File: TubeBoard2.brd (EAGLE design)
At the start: 155 x 114 mm, 2 parts

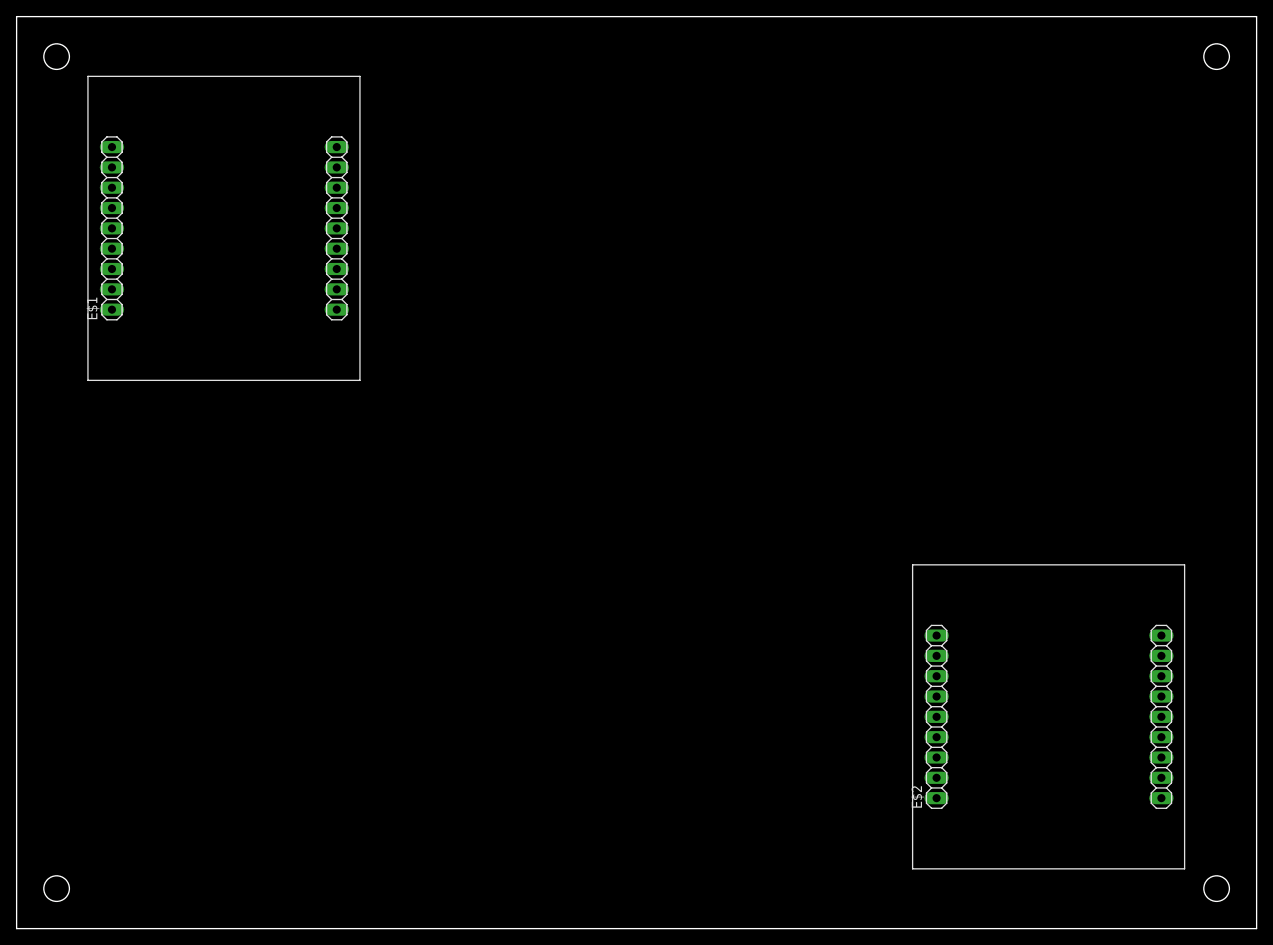
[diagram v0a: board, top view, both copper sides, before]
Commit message: [fix]真空管の場所を少し変更
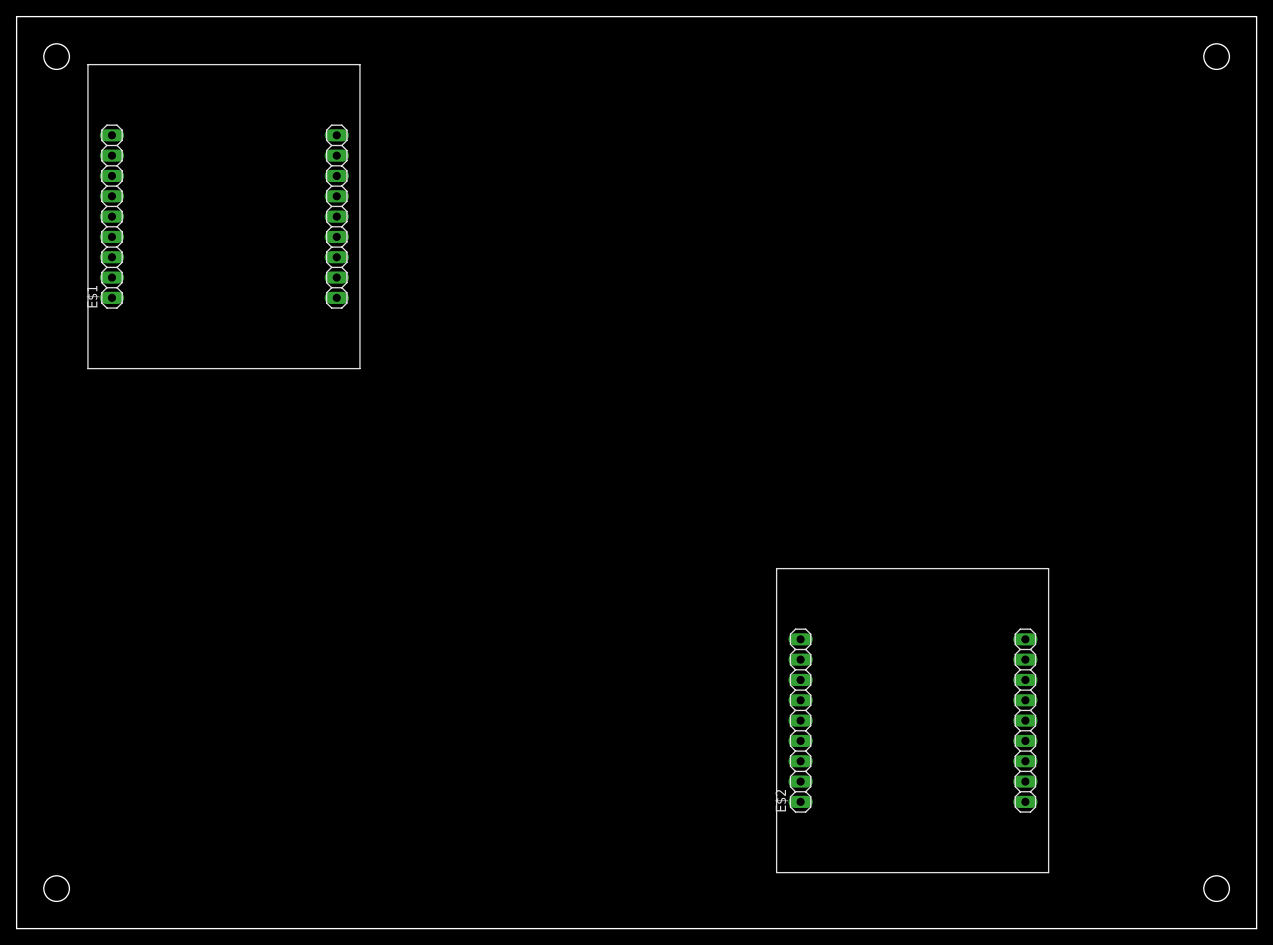
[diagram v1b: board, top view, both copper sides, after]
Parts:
- moved E$2 17.0 mm to (129.0, 7.00)
- moved E$1 1.47 mm to (42.9, 70.0)
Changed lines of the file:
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@@
 <drawing>
 <settings>
-<setting alwaysvectorfont="no"/>
+<setting alwaysvectorfont="yes"/>
 <setting verticaltext="up"/>
 </settings>
@@
 </layers>
 <board>
-<fusionsync huburn="a.cGVyc29uYWw6dWUyZDlmMDVj" projecturn="a.cGVyc29uYWw6dWUyZDlmMDVjIzIwMTgxMjMwMTY3NjU5OTU2" f3durn="urn:adsk.wipprod:dm.lineage:fGyzUlU2QBu9tUrGYZlviQ" pcbguid="c0a0ce5a-1e51-4658-88d9-be66126aa057" lastpulledtime="" lastsyncedchangeguid="f38ecf19-1331-d8f8-b58b-cd361b5029e6"/>
+<fusionsync huburn="a.cGVyc29uYWw6dWUyZDlmMDVj" projecturn="a.cGVyc29uYWw6dWUyZDlmMDVjIzIwMTgxMjMwMTY3NjU5OTU2" f3durn="urn:adsk.wipprod:dm.lineage:DSz6rBeQS9ylMETaIm7xKw" pcbguid="c46e325d-9af0-4786-afaf-edcf28a58fd8" lastpulledtime="" lastsyncedchangeguid="48b02016-af15-4da8-6dae-3d27a5383ea5"/>
 <plain>
 <wire x1="0" y1="0" x2="155" y2="0" width="0.1524" layer="20"/>
@@
 </autorouter>
 <elements>
-<element name="E$1" library="VacuumTube" library_urn="urn:adsk.eagle:library:8044196" package="AT-MT9P" package3d_urn="urn:adsk.eagle:package:8092351/8" value="" x="42.92" y="68.53" smashed="yes" rot="R90">
-<attribute name="NAME" x="38.1912" y="76.0238" size="1.27" layer="25" ratio="10" rot="R90"/>
-<attribute name="NAME" x="10.0912" y="76.0238" size="1.27" layer="25" ratio="10" rot="R90"/>
-<attribute name="VALUE" x="43.195" y="76.1" size="1.27" layer="27" rot="R90"/>
-<attribute name="VALUE" x="15.095" y="76.1" size="1.27" layer="27" rot="R90"/>
+<element name="E$1" library="VacuumTube" library_urn="urn:adsk.eagle:library:8044196" package="AT-MT9P" package3d_urn="urn:adsk.eagle:package:8092351/9" value="" x="42.92" y="70" smashed="yes" rot="R90">
+<attribute name="NAME" x="38.1912" y="77.4938" size="1.27" layer="25" ratio="10" rot="R90"/>
+<attribute name="NAME" x="10.0912" y="77.4938" size="1.27" layer="25" ratio="10" rot="R90"/>
+<attribute name="VALUE" x="43.195" y="77.57" size="1.27" layer="27" rot="R90"/>
+<attribute name="VALUE" x="15.095" y="77.57" size="1.27" layer="27" rot="R90"/>
 </element>
-<element name="E$2" library="VacuumTube" library_urn="urn:adsk.eagle:library:8044196" package="AT-MT9P" package3d_urn="urn:adsk.eagle:package:8092351/8" value="" x="146" y="7.47" smashed="yes" rot="R90">
-<attribute name="NAME" x="141.2712" y="14.9638" size="1.27" layer="25" ratio="10" rot="R90"/>
-<attribute name="NAME" x="113.1712" y="14.9638" size="1.27" layer="25" ratio="10" rot="R90"/>
-<attribute name="VALUE" x="146.275" y="15.04" size="1.27" layer="27" rot="R90"/>
-<attribute name="VALUE" x="118.175" y="15.04" size="1.27" layer="27" rot="R90"/>
+<element name="E$2" library="VacuumTube" library_urn="urn:adsk.eagle:library:8044196" package="AT-MT9P" package3d_urn="urn:adsk.eagle:package:8092351/9" value="" x="129" y="7" smashed="yes" rot="R90">
+<attribute name="NAME" x="124.2712" y="14.4938" size="1.27" layer="25" ratio="10" rot="R90"/>
+<attribute name="NAME" x="96.1712" y="14.4938" size="1.27" layer="25" ratio="10" rot="R90"/>
+<attribute name="VALUE" x="129.275" y="14.57" size="1.27" layer="27" rot="R90"/>
+<attribute name="VALUE" x="101.175" y="14.57" size="1.27" layer="27" rot="R90"/>
 </element>
 </elements>
